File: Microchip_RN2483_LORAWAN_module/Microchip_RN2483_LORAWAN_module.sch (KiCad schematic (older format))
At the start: 9 parts, among them P1 SMA_mini, U1 RN2483, U2 wireless_patice

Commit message: lorawan module PCB added, reorganized folders
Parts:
- SJ1, SJ2: footprint lorawan_module:solderjumper_bottom -> lorawan_module:solder_jumper_bott
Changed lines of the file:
@@
 encoding utf-8
 Sheet 1 1
-Title ""
-Date ""
-Rev ""
-Comp ""
+Title "Lorawan SNPM module"
+Date "2017-11-22"
+Rev "XXX"
+Comp "created by i_a"
 Comment1 ""
 Comment2 ""
@@
 F 0 "SJ1" H 5850 4250 60  0000 C CNN
 F 1 "solder_jumper" H 5800 4050 60  0001 C CNN
-F 2 "lorawan_module:solderjumper_bottom" H 5750 4150 60  0001 C CNN
+F 2 "lorawan_module:solder_jumper_bott" H 5750 4150 60  0001 C CNN
 F 3 "" H 5750 4150 60  0001 C CNN
 	1    5750 4150
@@
 F 0 "SJ2" H 6200 4350 60  0000 C CNN
 F 1 "solder_jumper" H 6150 4150 60  0001 C CNN
-F 2 "lorawan_module:solderjumper_bottom" H 6100 4250 60  0001 C CNN
+F 2 "lorawan_module:solder_jumper_bott" H 6100 4250 60  0001 C CNN
 F 3 "" H 6100 4250 60  0001 C CNN
 	1    6100 4250

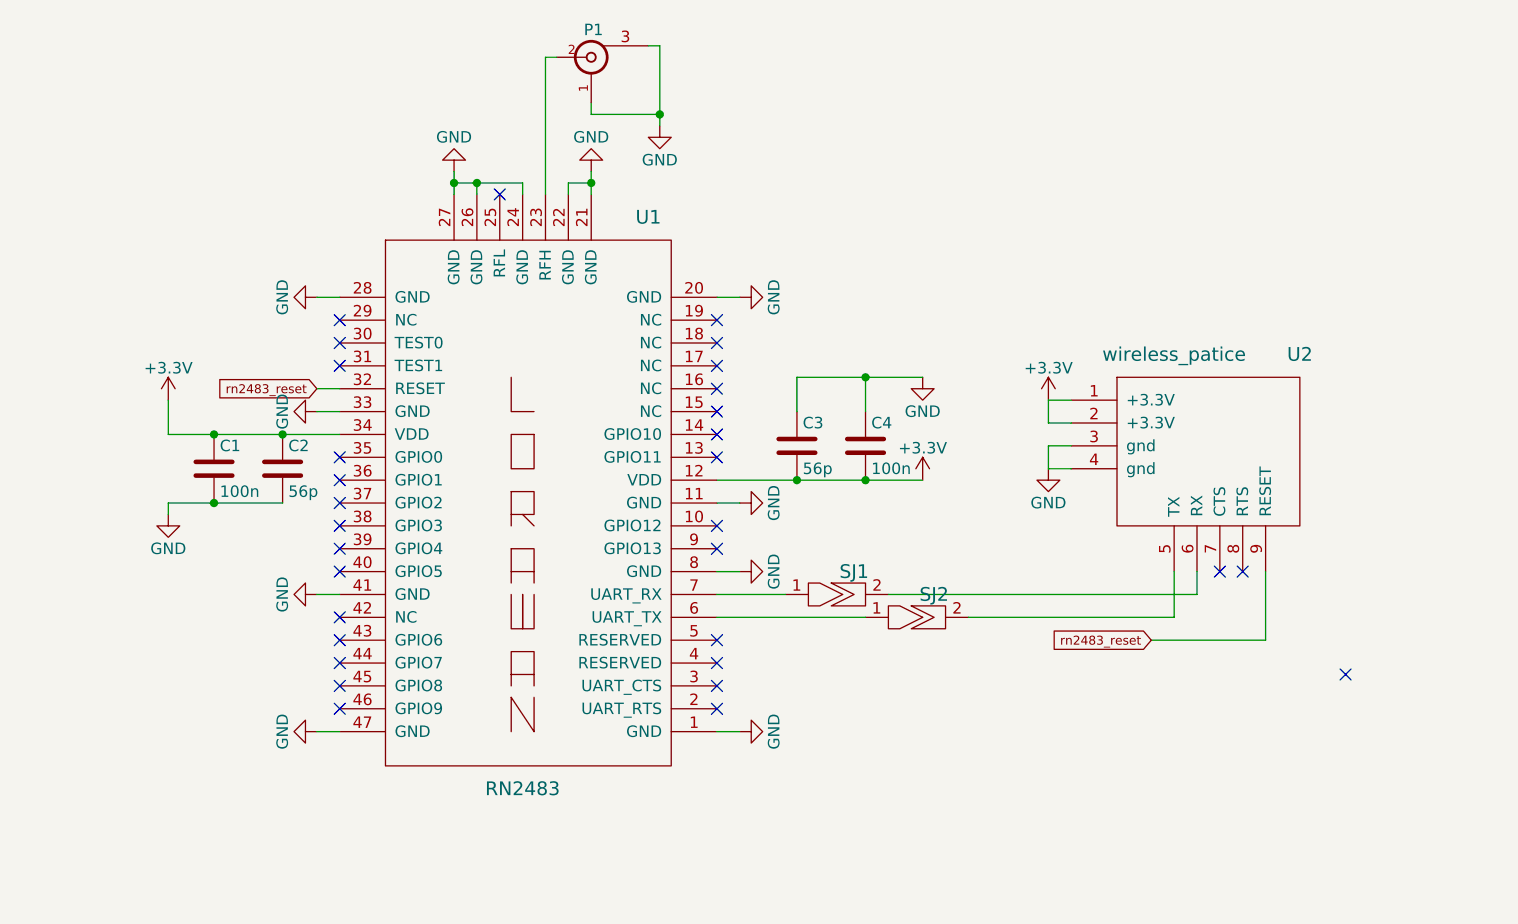
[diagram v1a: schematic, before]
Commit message: objednavka snpm a microchip redukce
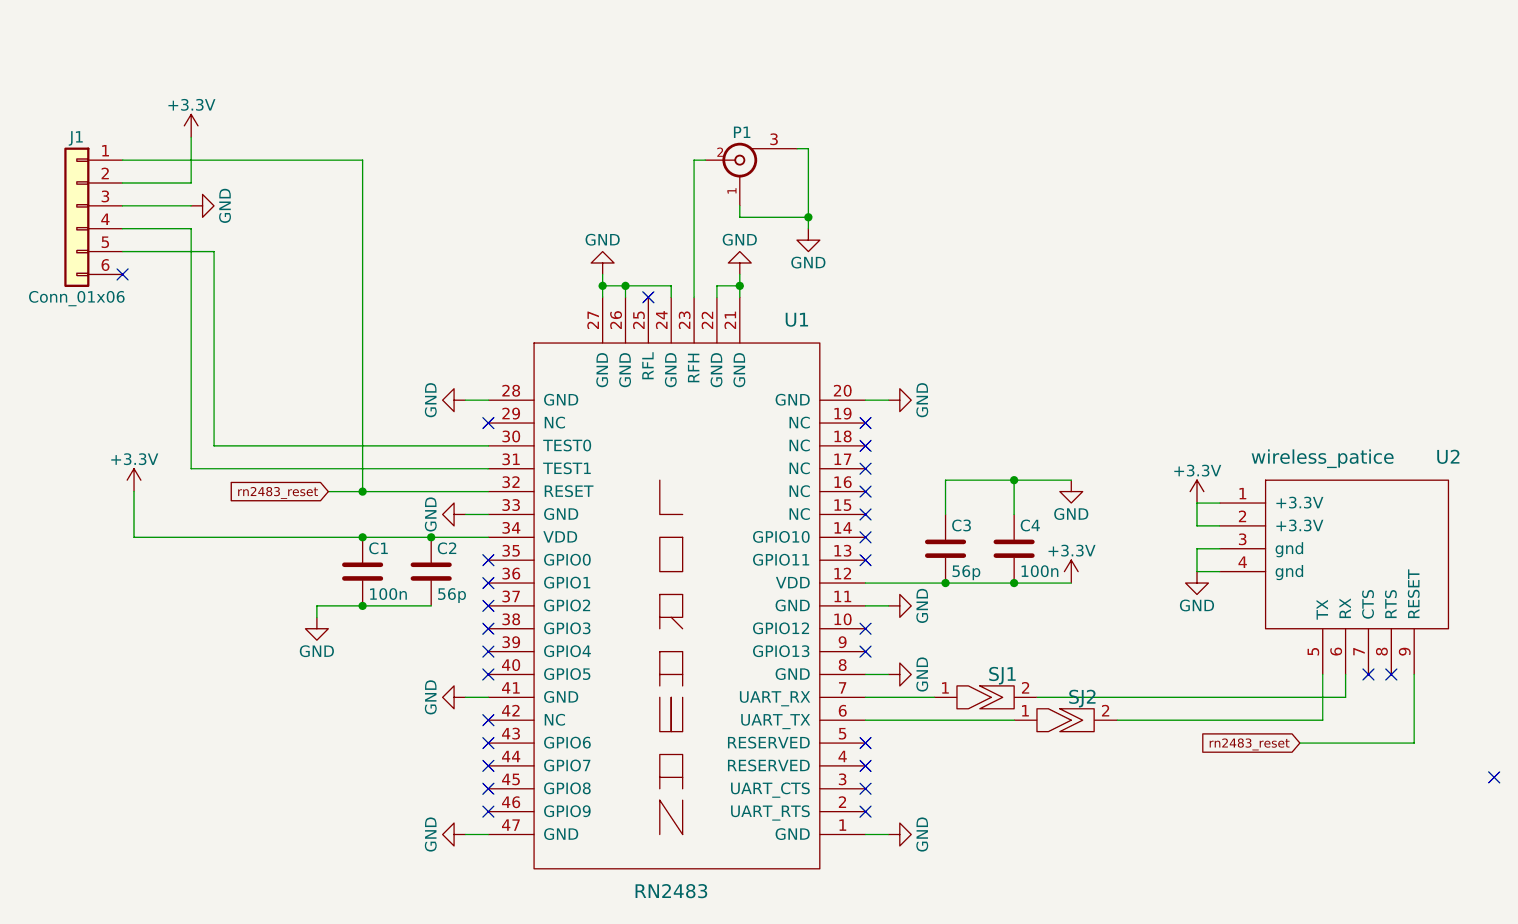
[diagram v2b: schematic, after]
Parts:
- added J1: Conn_01x06, lorawan_module:Pin_Header_Straight_1x06_Pitch2.54mm, symbol Conn_01x06
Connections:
- net +3V3: now also J1.2 (Pin_2)
- net GND: now also J1.3 (Pin_3)
- net rn2483_reset: now also J1.1 (Pin_1)
- net at U1.30 (TEST0): now also J1.5 (Pin_5)
- net at U1.31 (TEST1): now also J1.4 (Pin_4)
- no-connect marks 31 -> 30
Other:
- moved on the sheet: C1, C2, C3, C4, P1, SJ1, SJ2, U1, U2
